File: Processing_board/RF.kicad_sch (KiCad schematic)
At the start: 13 parts, among them J10 CONMHF1-SMD-G-T, U8 BGS13SN8E6327XTSA1

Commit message: created BOM, deleted useless folder Components and renamed CAD_Models to Parts
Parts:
- AE2: Link (none) -> https://www.mouser.ch/ProductDetail/ABRACON/AMCA31-2R450G-S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; MANUFACTURER (none) -> ABRACON; Panier (none) -> 1
- C34: Link (none) -> https://www.mouser.ch/ProductDetail/Murata-Electronics/GRM1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; MANUFACTURER (none) -> Murata Electronics; Manufacturer_Part_Number (none) -> GRM1555C1HR80BA01D; Panier (none) -> 1
- C35: Link (none) -> https://www.mouser.ch/ProductDetail/Murata-Electronics/GRM1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; MANUFACTURER (none) -> Murata Electronics; Manufacturer_Part_Number (none) -> GRM1555C1HR30WA01D; Panier (none) -> 1
- C38: Link (none) -> https://www.mouser.ch/ProductDetail/Walsin/0402N1R5B100CT?q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; MANUFACTURER (none) -> Walsin; Manufacturer_Part_Number (none) -> 0402N1R5B100CT; Panier (none) -> 1
- FL1: Link (none) -> https://www.mouser.ch/ProductDetail/TDK/DLF162500LT-5028A1?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; MANUFACTURER (none) -> TDK; Panier (none) -> 1
- J10: Link (none) -> https://www.mouser.ch/ProductDetail/TE-Connectivity-Linx-Te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; MANUFACTURER (none) -> TE Connectivity / Linx Technologies; Panier (none) -> 1
- L1: Link (none) -> https://www.mouser.ch/ProductDetail/Murata-Electronics/LQG1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; MANUFACTURER (none) -> Murata Electronics; Manufacturer_Part_Number (none) -> LQG15HS2N7S02D; Panier (none) -> 1
- L2: Link (none) -> https://www.mouser.ch/ProductDetail/TE-Connectivity-Sigma-I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; MANUFACTURER (none) -> TE Connectivity / Sigma Inductors; Manufacturer_Part_Number (none) -> 36550402S3N9T; Panier (none) -> 1
- U8: Link (none) -> https://www.mouser.ch/ProductDetail/Infineon-Technologies/B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; MANUFACTURER (none) -> Infineon Technologies; Panier (none) -> 1

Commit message: feat: finalized ADC design
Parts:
- C34, C35, C38: footprint Capacitor_SMD:C_0402_1005Metric -> Capacitor_SMD:C_0201_0603Metric_Pad0.64x0.40mm_HandSolder
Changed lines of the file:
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@@
 			)
 		)
-		(property "Footprint" "Capacitor_SMD:C_0402_1005Metric"
+		(property "Footprint" "Capacitor_SMD:C_0201_0603Metric_Pad0.64x0.40mm_HandSolder"
 			(at 36.5252 72.39 0)
 			(effects
@@
 			)
 		)
-		(property "Footprint" "Capacitor_SMD:C_0402_1005Metric"
+		(property "Footprint" "Capacitor_SMD:C_0201_0603Metric_Pad0.64x0.40mm_HandSolder"
 			(at 55.5752 72.39 0)
 			(effects
@@
 			)
 		)
-		(property "Footprint" "Capacitor_SMD:C_0402_1005Metric"
+		(property "Footprint" "Capacitor_SMD:C_0201_0603Metric_Pad0.64x0.40mm_HandSolder"
 			(at 219.4052 76.2 0)
 			(effects

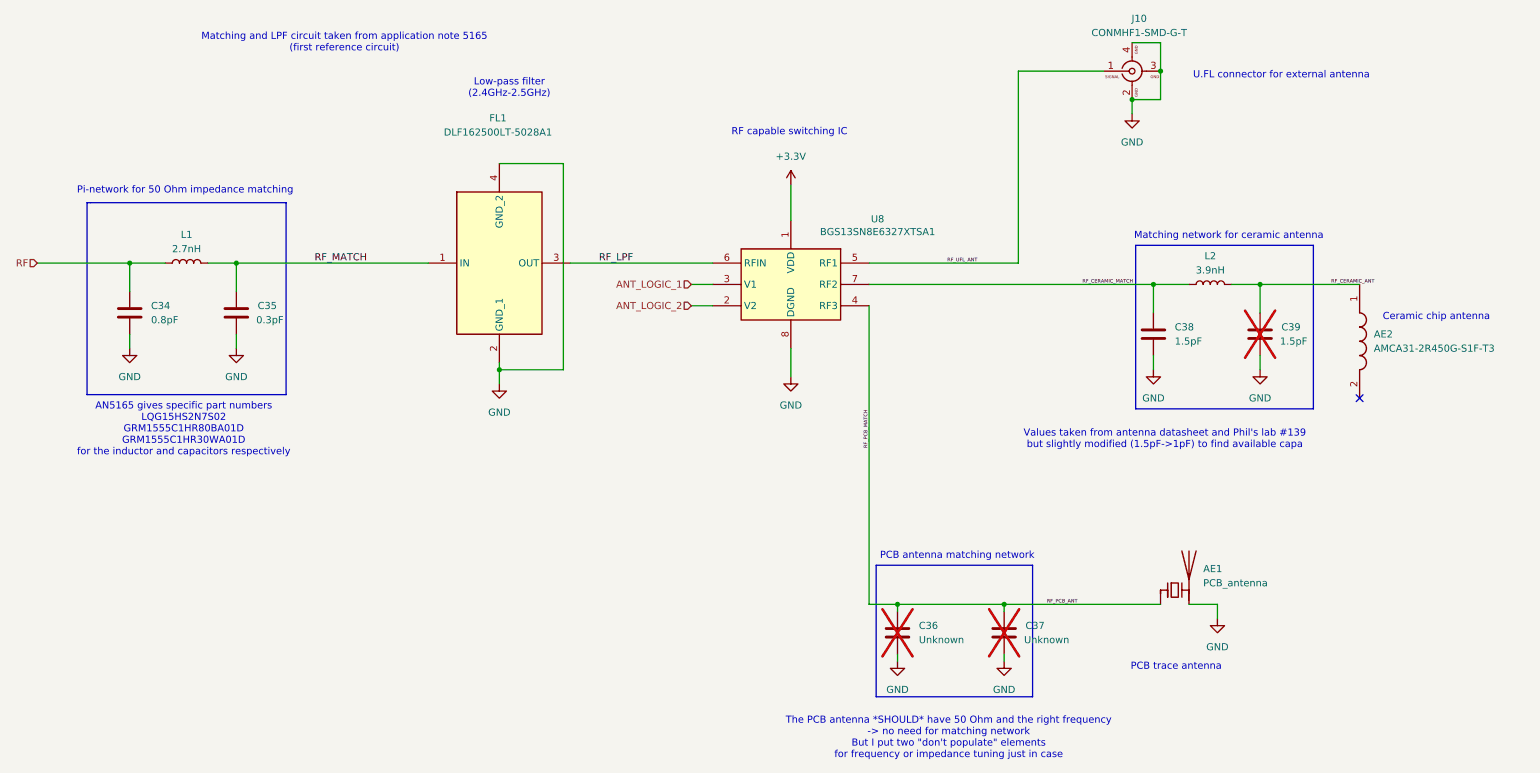
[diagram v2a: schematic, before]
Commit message: fix: changed back silkscreen
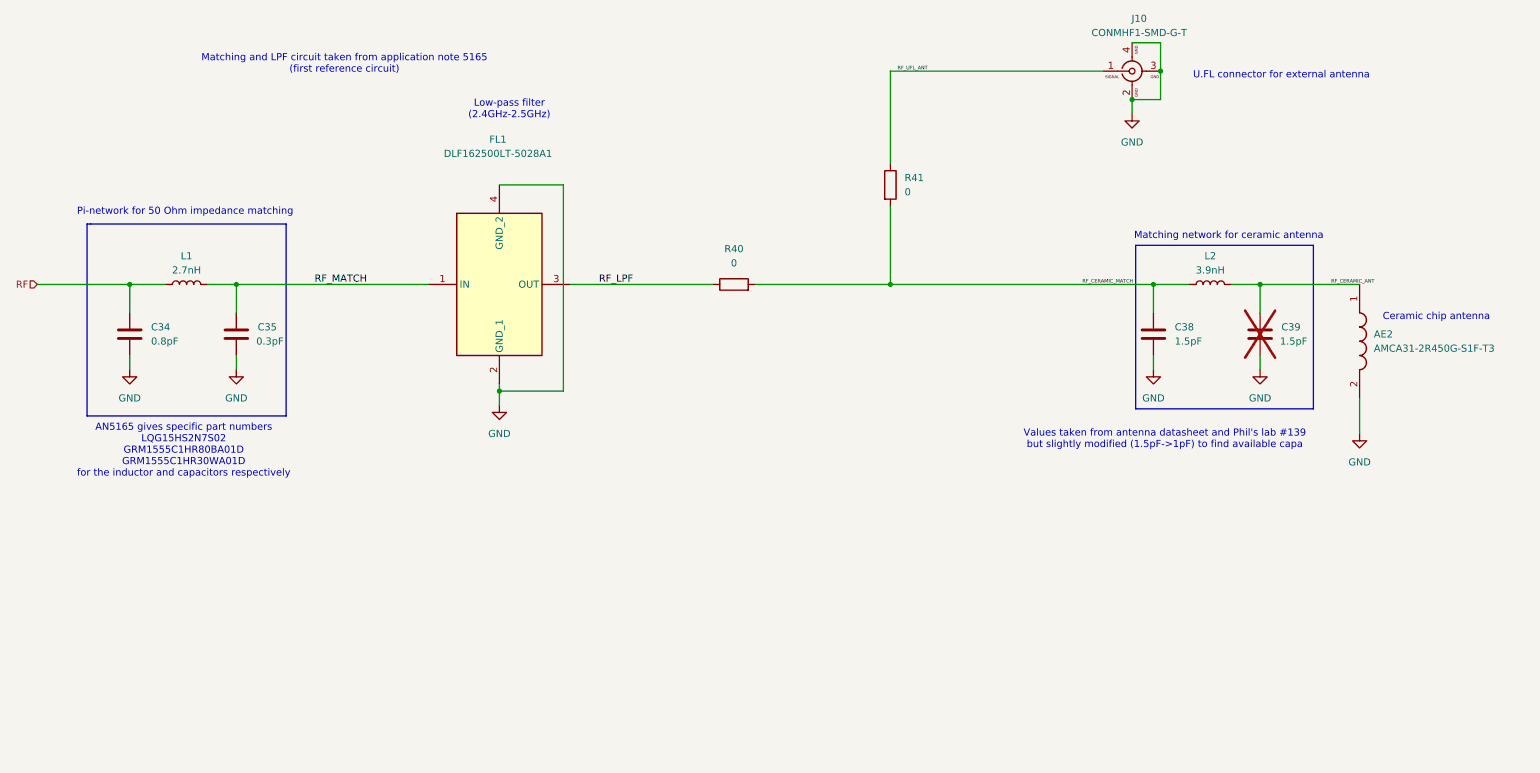
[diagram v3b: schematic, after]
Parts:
- removed AE1: PCB_antenna, RF_Antenna:Texas_SWRA117D_2.4GHz_Left, symbol Device:Antenna_Chip
- removed C36, C37: Unknown, Capacitor_SMD:C_0402_1005Metric, symbol Device:C
- removed U8: BGS13SN8E6327XTSA1, BGS13SN8E6327XTSA1:BGS13SN8E6327XTSA1, symbol BGS13SN8E6327XTSA1:BGS13SN8E6327XTSA1
- added R40, R41: 0, Resistor_SMD:R_0603_1608Metric, symbol Device:R
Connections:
- net GND: now also AE2.2 (NC)
- net RF_CERAMIC_MATCH: now also R40.2, R41.2
- net RF_LPF: now also R40.1
- net RF_UFL_ANT: now also R41.1
- no-connect marks 1 -> 0
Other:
- note removed: "PCB antenna matching network"
- note removed: "PCB trace antenna"
- note removed: "RF capable switching IC"
- note removed: "The PCB antenna *SHOULD* have 50 Ohm and the right frequency -> no need for matching network But I put two "don't populate" elements for frequency or impedance tuning just in case"
- moved on the sheet: C34, C35, FL1, L1
